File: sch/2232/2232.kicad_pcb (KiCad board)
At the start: 2 copper layers, 58 parts, among them J1 47346-0001, J2 IDC-06, J3 IDC-06, J4 IDC-10, J5 IDC-10, J6 6P6C, J7 Screw_Terminal_01x06, J8 Screw_Terminal_01x06, U1 FT2232D, U2 AMS1117-3.3, U3 ATmega324A-AU, U4 74LVC244AP, U5 74LVC244AP, U6 ST232BD, U7 74HC138, Y1 6 MHz, Y2 16 MHz

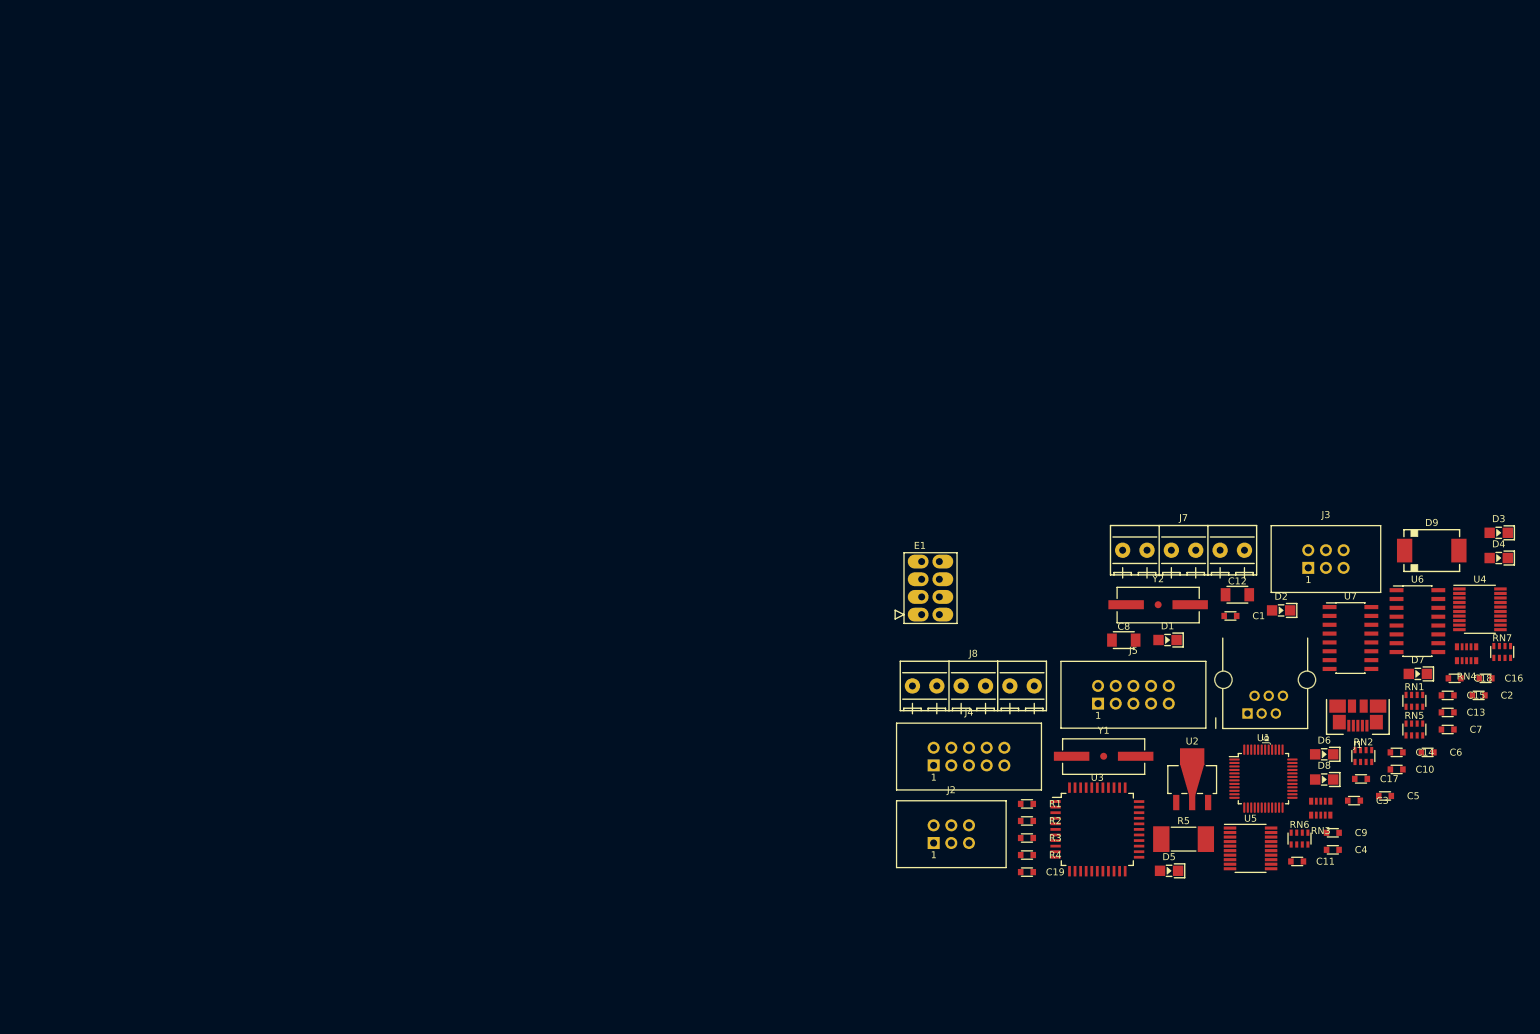
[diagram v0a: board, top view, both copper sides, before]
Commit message: PCB orientation stub
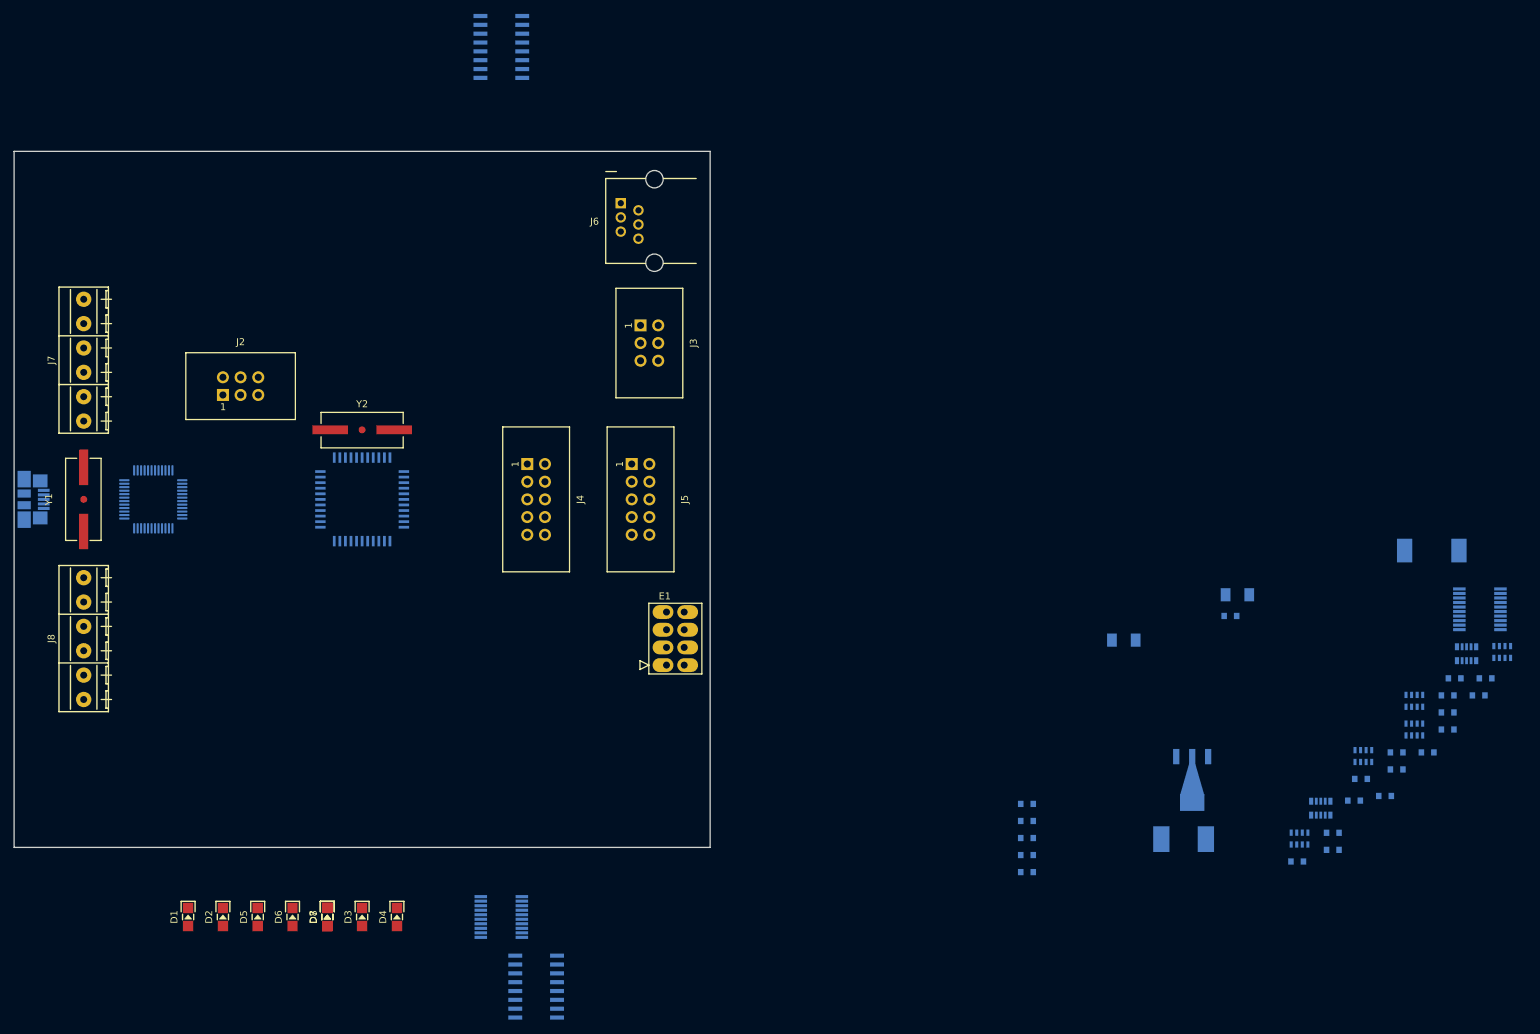
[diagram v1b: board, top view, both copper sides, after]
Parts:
- C1, C10, C11, C12, C13, C14, C15, C16, C17, C18, C19, C2, C3, C4, C5, C6, C7, C8, C9, D9, J1, R1, R2, R3, R4, R5, RN1, RN2, RN3, RN4, RN5, RN6, RN7, U1, U2, U3, U4, U5, U6, U7: moved to B.Cu
- moved J1 195.1 mm to (50.0, 100.0), turned to 270 degrees
- moved D3 172.4 mm to (100.0, 160.0), turned to 90 degrees
- moved D4 166.5 mm to (105.0, 160.0), turned to 90 degrees
- moved U1 164.5 mm to (70.0, 100.0)
- moved D7 160.5 mm to (95.0, 160.0), turned to 90 degrees
- moved J7 160.4 mm to (60.0, 80.0), turned to 90 degrees
- moved D2 158.3 mm to (80.0, 160.0), turned to 90 degrees
- moved U6 155.3 mm to (120.0, 35.0)
- moved Y1 151.1 mm to (60.0, 100.0), turned to 270 degrees
- moved D6 150.1 mm to (90.0, 160.0), turned to 90 degrees
- moved D1 146.2 mm to (75.0, 160.0), turned to 90 degrees
- moved D8 144.6 mm to (95.0, 160.0), turned to 90 degrees
- moved D5 131.1 mm to (85.0, 160.0), turned to 90 degrees
- moved J8 128.0 mm to (60.0, 120.0), turned to 90 degrees
- moved U7 127.3 mm to (125.0, 170.0)
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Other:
- board outline added: 100 x 100 mm

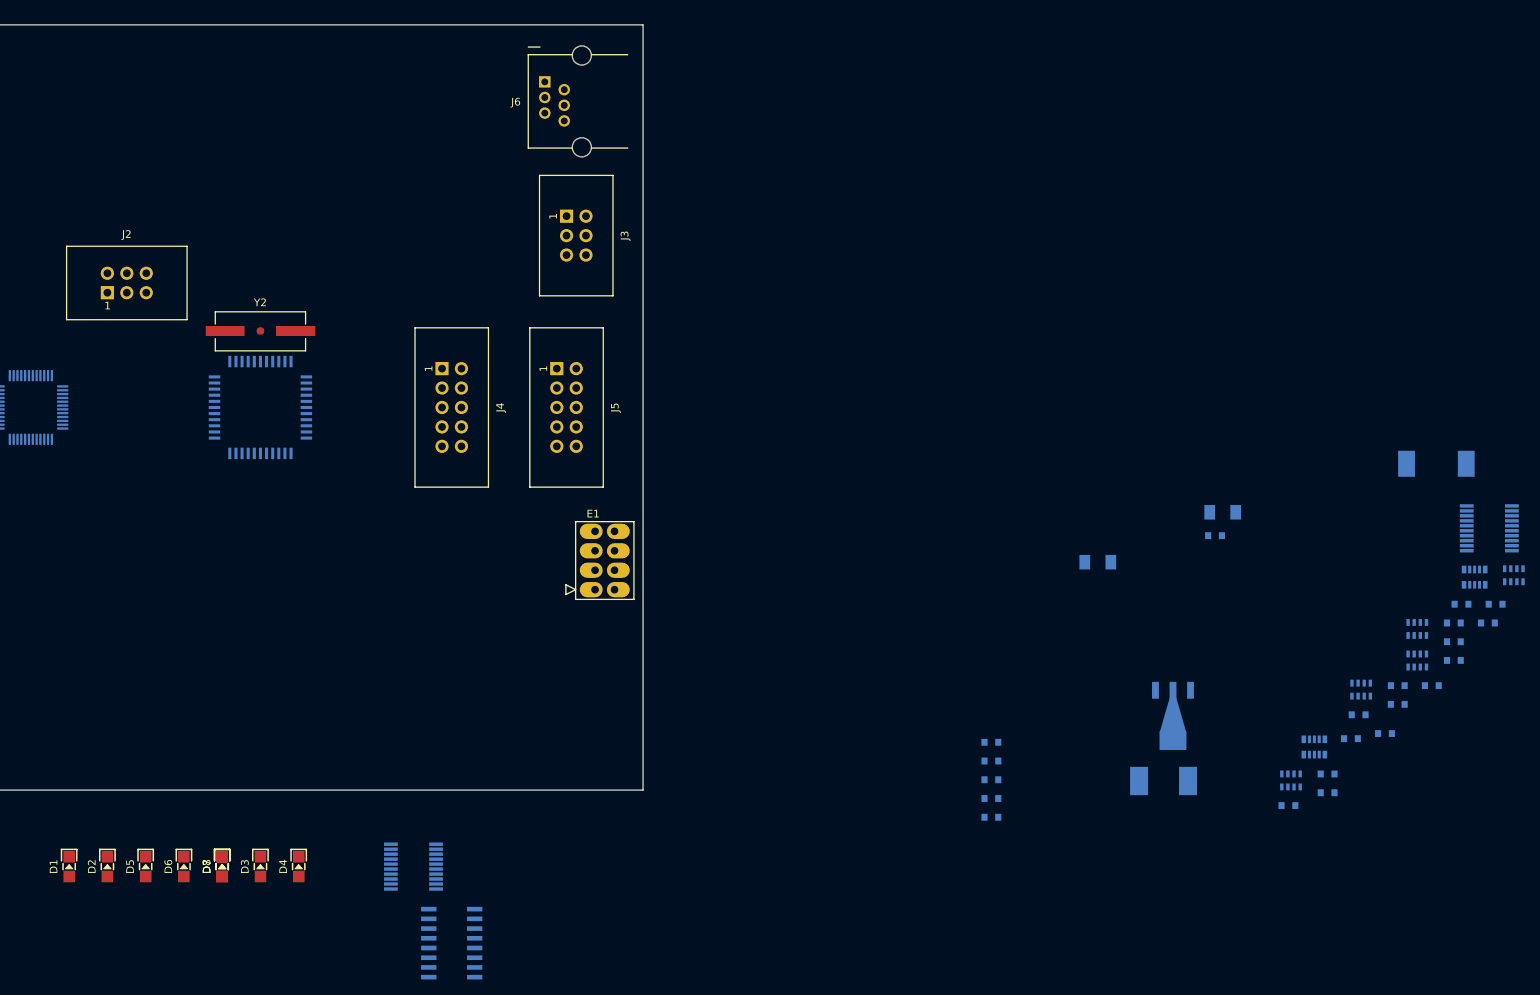
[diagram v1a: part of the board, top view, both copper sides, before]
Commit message: UART multiplexing
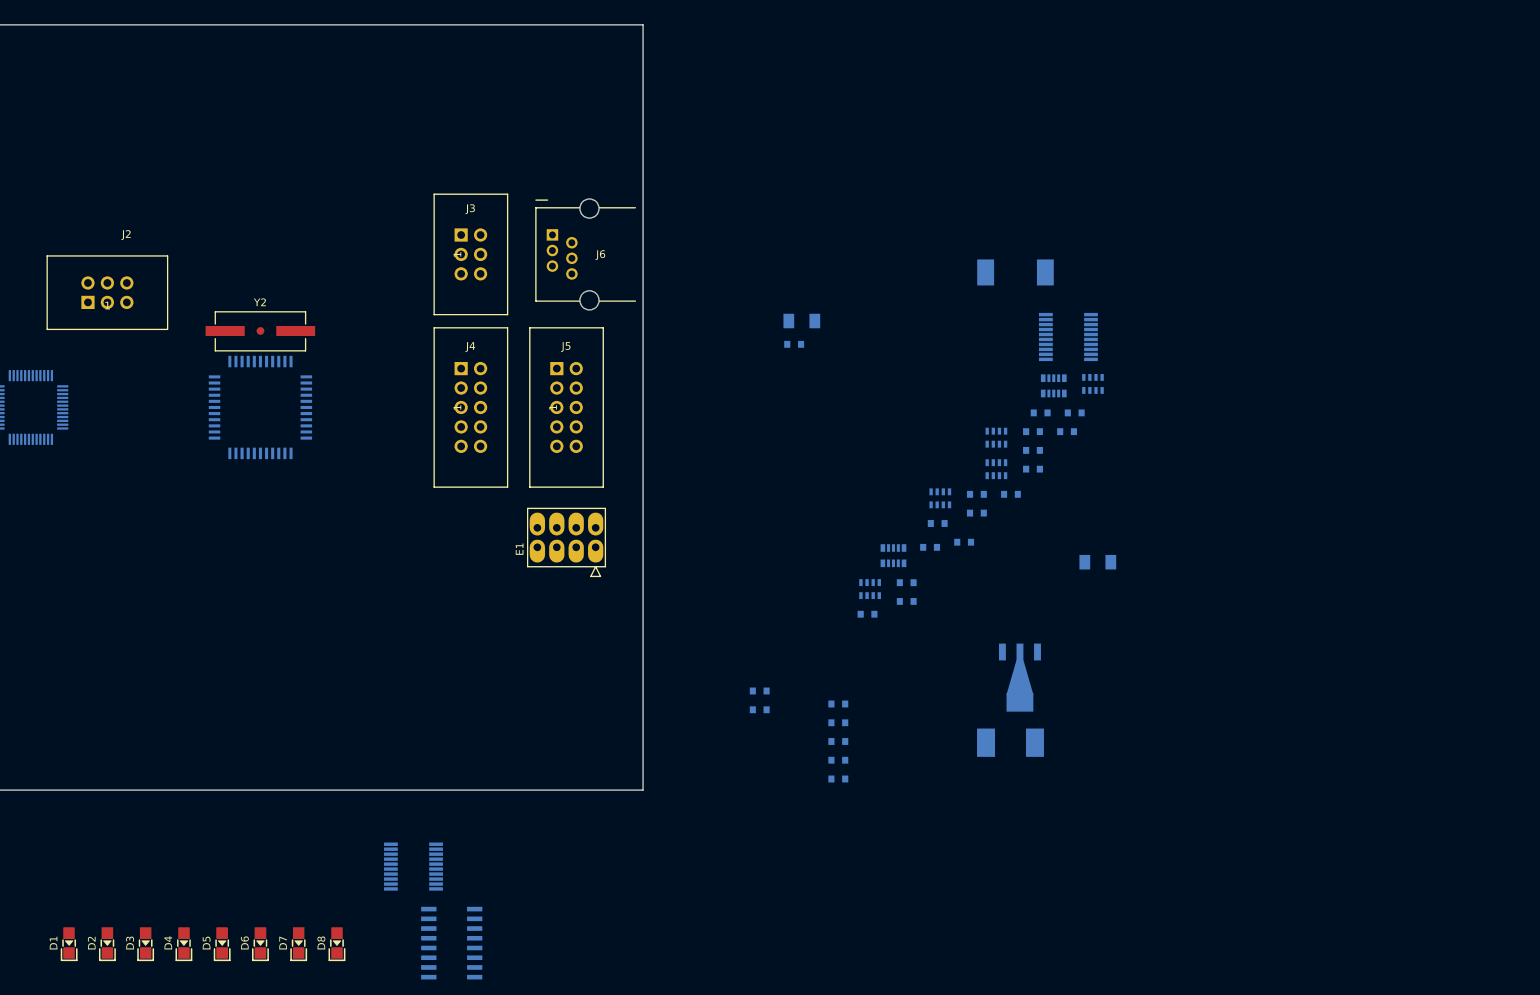
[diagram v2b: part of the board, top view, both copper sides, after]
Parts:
- added R6: 1k, NevaDA:R_0603, B.Cu at (165.2, 139.5)
- added R7: 1k, NevaDA:R_0603, B.Cu at (165.2, 137.1)
- E1: value ESP-01 -> WIFI
- RN1, RN2: value CAT16-471J4 -> CAT16-102J4
- moved C16 60.4 mm to (206.4, 100.7)
- moved C2 60.4 mm to (205.4, 103.2)
- moved RN7 60.4 mm to (208.8, 96.9)
- moved C10 60.4 mm to (193.6, 113.8)
- moved C11 60.4 mm to (179.3, 127.0)
- moved C13 60.4 mm to (201.0, 105.6)
- moved C5 60.4 mm to (192.0, 117.6)
- moved RN3 60.4 mm to (182.7, 119.4)
- moved RN6 60.4 mm to (179.7, 123.7)
- moved C1 60.4 mm to (169.8, 91.8)
- moved C12 60.4 mm to (170.8, 88.7)
- moved C14 60.4 mm to (193.6, 111.3)
- moved C15 60.4 mm to (201.0, 103.2)
- moved C17 60.4 mm to (188.5, 115.2)
- moved C3 60.4 mm to (187.5, 118.3)
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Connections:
- RN2 pad 4: /EN_UART_RS -> (no net)
- U4 pad 13: /PAR_0_T2 -> /TX2_3V
- U4 pad 17: /FSCK_T1 -> /TX1_3V
- U4 pad 19: /EN_UART_RS -> /EN_UART_3V
- U4 pad 5: /FDO_R1 -> Net-(R6-Pad2)
- U4 pad 9: /PAR_1_R2 -> Net-(R7-Pad2)

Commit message: Routing started
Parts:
- removed U7: 74HC138, NevaDA:SOIC-16
- added R10: 1M, NevaDA:R_0603, B.Cu at (63.5, 94.2)
- added V1: Virtual, NevaDA:StickyPad_13mm, B.Cu at (76.0, 73.5)
- added V2: Virtual, NevaDA:StickyPad_13mm, B.Cu at (76.0, 126.5)
- added V3: Virtual, NevaDA:StickyPad_13mm, B.Cu at (125.0, 73.5)
- added V4: Virtual, NevaDA:StickyPad_13mm, B.Cu at (125.0, 126.5)
- E1: value WIFI -> ESP-01
- moved R5 136.1 mm to (67.0, 107.0), turned to 180 degrees
- moved C6 122.8 mm to (76.5, 93.8), turned to 180 degrees
- moved D9 119.3 mm to (89.5, 130.5), turned to 180 degrees
- moved C3 116.4 mm to (72.5, 100.2), turned to 180 degrees
- moved R2 114.4 mm to (69.0, 99.5), turned to 180 degrees
- moved RN3 114.0 mm to (73.3, 87.5)
- moved R1 113.0 mm to (69.0, 101.0), turned to 180 degrees
- moved C5 112.3 mm to (80.0, 108.8), turned to 180 degrees
- moved C4 108.5 mm to (77.5, 107.0), turned to 270 degrees
- moved R4 103.1 mm to (80.0, 107.2), turned to 180 degrees
- moved J2 57.6 mm to (35.0, 121.0), turned to 270 degrees
- moved U5 49.1 mm to (109.5, 112.0)
- moved D1 40.4 mm to (80.5, 130.0)
- moved D8 40.3 mm to (105.0, 130.0)
- moved D2 40.2 mm to (84.0, 130.0)
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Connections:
- net /USB_m renamed /USB_D-
- net /USB_p renamed /USB_D+
- net /USBf_m renamed /USBf_D-
- D1 pad 1: Net-(D1-Pad1) -> /LED1
- D1 pad 2: +5V -> Net-(D1-Pad2)
- D2 pad 1: Net-(D2-Pad1) -> /LED2
- D2 pad 2: +5V -> Net-(D2-Pad2)
- D3 pad 1: Net-(D3-Pad1) -> /LED3_~RD
- D3 pad 2: +5V -> Net-(D3-Pad2)
- D4 pad 1: Net-(D4-Pad1) -> /LED4_~WR
- D4 pad 2: +5V -> Net-(D4-Pad2)
- D5 pad 1: Net-(D5-Pad1) -> /EN_UART
- D5 pad 2: +5V -> Net-(D5-Pad2)
- D6 pad 1: Net-(D6-Pad1) -> /FBUFF
- D6 pad 2: +5V -> Net-(D6-Pad2)
- D7 pad 1: Net-(D7-Pad1) -> /MCU_BUFF
- D7 pad 2: +5V -> Net-(D7-Pad2)
- D8 pad 1: Net-(D8-Pad1) -> /MCU_LED
- D8 pad 2: +5V -> Net-(D8-Pad2)
- R2 pad 1: /USBf_p -> /USBf_D+
- R3 pad 2: /USBf_p -> (no net)
- RN1 pad 1: /LED1 -> +5V
- RN1 pad 2: /LED2 -> +5V
- RN1 pad 3: /LED3_~RD -> +5V
- RN1 pad 4: /LED4_~WR -> +5V
- RN1 pad 5: Net-(D4-Pad1) -> Net-(D1-Pad2)
- RN1 pad 6: Net-(D3-Pad1) -> Net-(D2-Pad2)
- RN1 pad 7: Net-(D2-Pad1) -> Net-(D3-Pad2)
- RN1 pad 8: Net-(D1-Pad1) -> Net-(D4-Pad2)
- RN2 pad 1: /FBUFF -> +5V
- RN2 pad 2: /MCU_BUFF -> +5V
- RN2 pad 3: /EN_UART_3V -> +5V
- RN2 pad 4: (no net) -> +5V
- RN2 pad 5: Net-(D8-Pad1) -> Net-(D5-Pad2)
- RN2 pad 6: Net-(D7-Pad1) -> Net-(D6-Pad2)
- RN2 pad 7: Net-(D6-Pad1) -> Net-(D7-Pad2)
- RN2 pad 8: Net-(D5-Pad1) -> Net-(D8-Pad2)
- U1 pad 16: (no net) -> /LED4_~WR
- U1 pad 17: (no net) -> /LED3_~RD
- U1 pad 29: (no net) -> /PAR_~TXE
- U1 pad 30: (no net) -> /PAR_~RXF
- U1 pad 7: /USBf_p -> /USBf_D+
- U3 pad 11: (no net) -> /PAR_~RXF
- U3 pad 12: (no net) -> /PAR_~TXE
- U3 pad 13: (no net) -> /LED3_~RD
- U3 pad 14: (no net) -> /LED4_~WR
- U3 pad 15: (no net) -> /USB_reset
- U3 pad 16: (no net) -> /MCU_LED
- U3 pad 43: (no net) -> /MCU_BUFF
- U3 pad 7: (no net) -> Net-(C10-Pad1)
- U4 pad 1: /EN_UART_3V -> /EN_UART
- U4 pad 19: /EN_UART_3V -> /EN_UART
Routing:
- net GNDD: track 0.00 -> 21.2 mm, vias 0 -> 6
- net VCC: track 0.00 -> 20.4 mm
- net +5V: track 0.00 -> 16.8 mm
- net Net-(J1-Pad5): track 0.00 -> 14.4 mm
- net /USBf_D-: track 0.00 -> 9.82 mm
- net Net-(C2-Pad1): track 0.00 -> 6.46 mm, vias 0 -> 1
- net Net-(C1-Pad1): track 0.00 -> 6.46 mm, vias 0 -> 1
- net /USBf_D+: track 0.00 -> 6.08 mm
- net Net-(C4-Pad1): track 0.00 -> 4.66 mm
- net /USB_D+: track 0.00 -> 4.05 mm
- net /USB_D-: track 0.00 -> 3.98 mm
- net Net-(C3-Pad1): track 0.00 -> 2.44 mm
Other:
- board size 100 x 100 mm -> 80 x 70 mm
- board text added: "+12V"
- board text added: "+3.3V"
- board text added: "2232HIO"
- board text added: "2can"
- board text added: "CMOS/TTL"
- board text added: "ESP-01"
- board text added: "GND"
- board text added: "ISP"
- board text added: "ISP (x2 in parallel)"
- board text added: "MPROG"
- board text added: "RS-232"
- board text added: "Rx1"
- board text added: "Rx2"
- board text added: "STATUS"
- board text added: "Tx1"
- board text added: "Tx2"
- board text added: "UART"
- board text added: "USB"
